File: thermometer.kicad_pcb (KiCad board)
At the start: 2 copper layers, 78.1 x 21.6 mm, 11 parts, among them IC1 ATTINY2313A-P, P1 CONN_4, P2 CONN_4, U1 MC78L05AACP

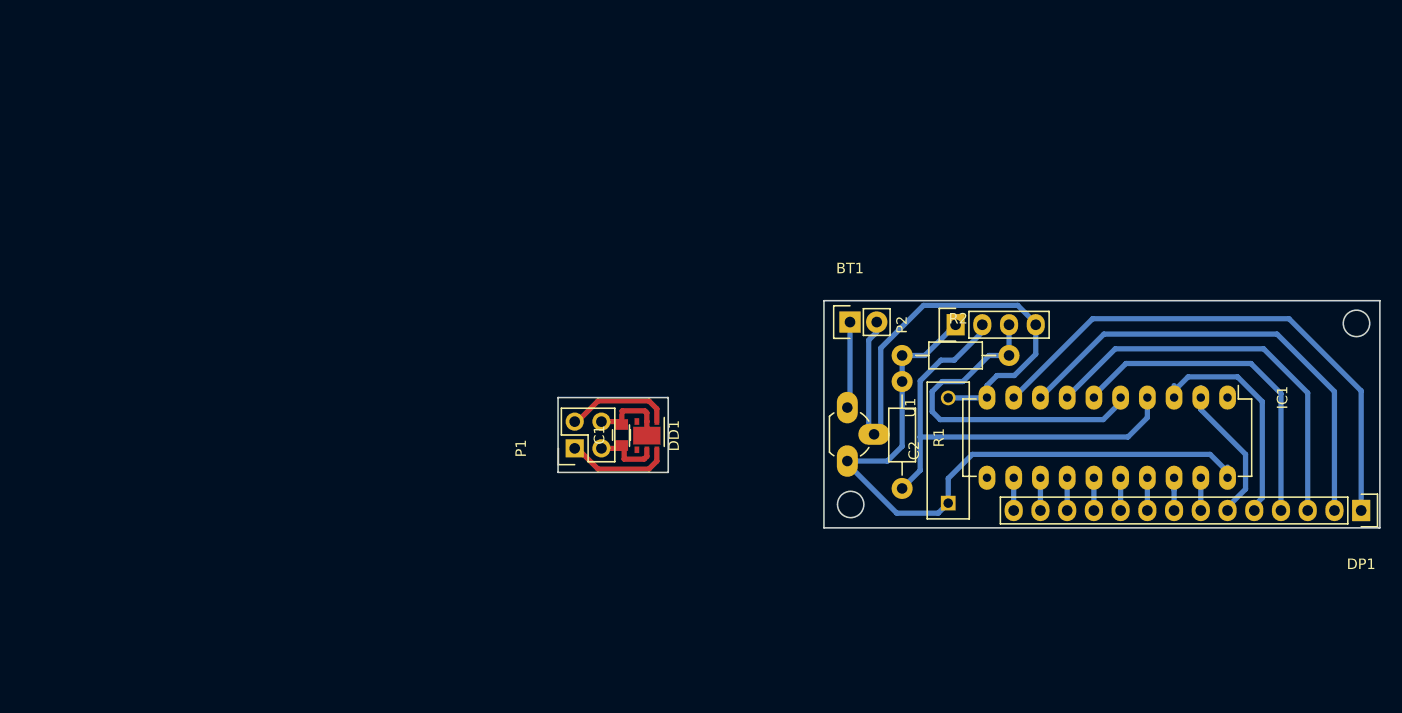
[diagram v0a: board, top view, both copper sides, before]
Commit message: Add I2C functions
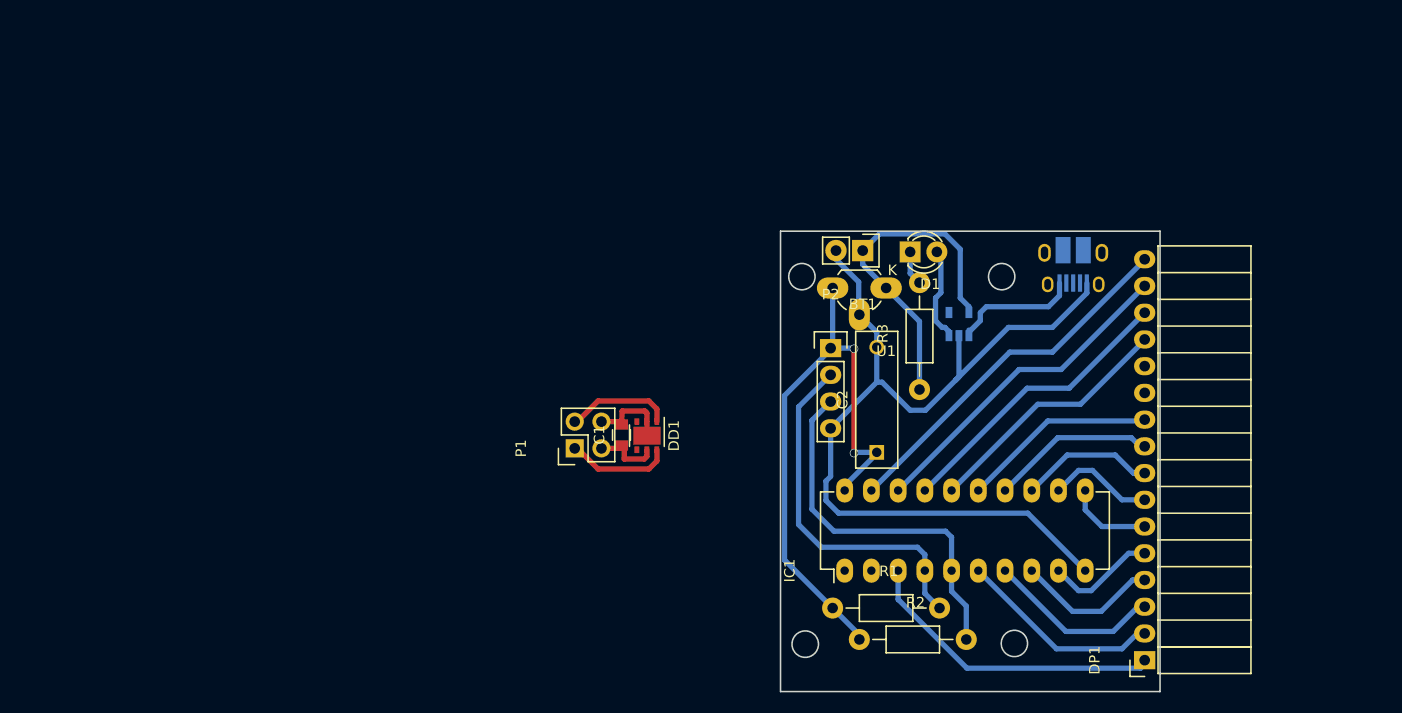
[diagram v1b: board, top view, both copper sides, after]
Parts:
- added D1: LED, LEDs:LED-3MM, F.Cu at (193.1, 96.5)
- added D2: max1555, TO_SOT_Packages_SMD:SOT-23-5, B.Cu at (197.7, 103.4)
- added P3: CONN_5, Connect:USB_Micro-B_10103594-0001LF, B.Cu at (208.6, 98.0)
- added R3: R, Resistors_ThroughHole:Resistor_Horizontal_RM10mm, F.Cu at (194.0, 109.6)
- DP1: footprint Socket_Strips:Socket_Strip_Straight_1x14 -> Socket_Strips:Socket_Strip_Angled_1x16
- moved IC1 39.9 mm to (186.9, 126.8), turned to 90 degrees
- moved R2 27.3 mm to (188.3, 133.3)
- moved DP1 25.0 mm to (215.4, 135.3), turned to 90 degrees
- moved R1 22.5 mm to (185.7, 130.4), turned to 0 degrees
- moved P2 12.1 mm to (185.5, 105.7), turned to 0 degrees
- moved U1 11.9 mm to (190.8, 99.9), turned to 180 degrees
- moved C2 8.33 mm to (189.9, 115.6)
- moved BT1 6.90 mm to (188.6, 96.4), turned to 180 degrees
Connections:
- C1 pad 1: VCC -> VDD
- DD1 pad 5: VCC -> VDD
- DP1 pad 11: Net-(DP1-Pad11) -> (no net)
- DP1 pad 12: Net-(DP1-Pad12) -> (no net)
- IC1 pad 11: (no net) -> Net-(DP1-Pad6)
- IC1 pad 12: Net-(DP1-Pad14) -> Net-(DP1-Pad7)
- IC1 pad 13: Net-(DP1-Pad13) -> Net-(DP1-Pad8)
- IC1 pad 14: Net-(DP1-Pad12) -> Net-(DP1-Pad9)
- IC1 pad 15: Net-(DP1-Pad11) -> Net-(DP1-Pad10)
- IC1 pad 16: Net-(DP1-Pad10) -> Net-(DP1-Pad13)
- IC1 pad 17: Net-(DP1-Pad9) -> Net-(DP1-Pad14)
- IC1 pad 18: Net-(DP1-Pad8) -> Net-(DP1-Pad15)
- IC1 pad 19: Net-(DP1-Pad7) -> Net-(DP1-Pad16)
- IC1 pad 2: Net-(DP1-Pad6) -> (no net)
- IC1 pad 3: Net-(DP1-Pad5) -> Net-(DP1-Pad1)
- IC1 pad 6: Net-(DP1-Pad4) -> Net-(DP1-Pad2)
- IC1 pad 8: Net-(DP1-Pad2) -> Net-(DP1-Pad4)
- IC1 pad 9: Net-(DP1-Pad1) -> Net-(DP1-Pad5)
- P1 pad 3: VCC -> VDD
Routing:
- net Net-(DP1-Pad16): track 0.00 -> 35.2 mm
- net GNDPWR: track 50.8 -> 85.8 mm
- net Net-(DP1-Pad15): track 0.00 -> 31.5 mm
- net Net-(DP1-Pad14): track 3.11 -> 27.9 mm
- net Net-(DP1-Pad2): track 44.0 -> 19.5 mm
- net Net-(BT1-Pad1): track 8.23 -> 32.3 mm
- net Net-(DP1-Pad13): track 3.11 -> 24.4 mm
- net Net-(DP1-Pad3): track 37.7 -> 16.6 mm
- net Net-(DP1-Pad1): track 50.3 -> 29.4 mm
- net Net-(DP1-Pad4): track 31.5 -> 13.6 mm
- net Net-(DP1-Pad10): track 3.11 -> 18.9 mm
- net Net-(DP1-Pad9): track 3.11 -> 15.7 mm
- net Net-(D2-Pad1): track 0.00 -> 12.5 mm
- net Net-(DP1-Pad5): track 22.4 -> 10.5 mm
- net Net-(IC1-Pad4): track 44.5 -> 34.3 mm
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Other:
- board size 78.1 x 21.6 mm -> 36.1 x 43.8 mm

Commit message: Add
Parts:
- added P4: CONN_4, Pin_Headers:Pin_Header_Straight_1x04, F.Cu at (160.7, 82.0)
- added R4: 10k, Resistors_ThroughHole:Resistor_Horizontal_RM7mm, F.Cu at (165.8, 93.6)
- added R5: 10k, Resistors_ThroughHole:Resistor_Horizontal_RM7mm, F.Cu at (168.8, 93.6)
- C2: footprint Capacitors_ThroughHole:C_Rect_L13_W4_P10 -> Capacitors_ThroughHole:C_Rect_L7_W2.5_P5
- DP1: value LCD_Display -> LCD_Display_5; footprint Socket_Strips:Socket_Strip_Angled_1x16 -> Socket_Strips:Socket_Strip_Angled_1x14
- R1, R2, R3: footprint Resistors_ThroughHole:Resistor_Horizontal_RM10mm -> Resistors_ThroughHole:Resistor_Horizontal_RM7mm
- moved C1 52.8 mm to (119.2, 88.8)
- moved DD1 52.8 mm to (121.6, 88.8)
- moved P1 52.8 mm to (114.7, 90.0)
- moved P3 51.4 mm to (158.1, 107.6), turned to 90 degrees
- moved R2 48.9 mm to (159.8, 93.6), turned to 90 degrees
- moved IC1 48.4 mm to (171.8, 80.8), turned to 0 degrees
- moved R1 43.3 mm to (162.8, 93.6), turned to 90 degrees
- moved DP1 39.6 mm to (182.8, 112.9)
- moved P2 36.8 mm to (156.8, 82.8)
- moved D1 35.4 mm to (157.8, 100.0), turned to 90 degrees
- moved D2 34.5 mm to (163.4, 106.3), turned to 0 degrees
- moved R3 29.1 mm to (165.8, 102.6), turned to 180 degrees
- moved BT1 26.1 mm to (166.4, 110.0)
- moved U1 24.0 mm to (167.1, 96.3)
- moved C2 13.7 mm to (179.4, 106.7), turned to 180 degrees
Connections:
- C1 pad 1: VDD -> VCC
- DD1 pad 5: VDD -> VCC
- DP1 pad 11: (no net) -> Net-(DP1-Pad11)
- DP1 pad 12: (no net) -> Net-(DP1-Pad11)
- DP1 pad 6: Net-(DP1-Pad6) -> (no net)
- IC1 pad 11: Net-(DP1-Pad6) -> Net-(DP1-Pad4)
- IC1 pad 12: Net-(DP1-Pad7) -> Net-(DP1-Pad5)
- IC1 pad 13: Net-(DP1-Pad8) -> Net-(DP1-Pad7)
- IC1 pad 14: Net-(DP1-Pad9) -> Net-(DP1-Pad8)
- IC1 pad 15: Net-(DP1-Pad10) -> Net-(DP1-Pad9)
- IC1 pad 16: Net-(DP1-Pad13) -> Net-(DP1-Pad10)
- IC1 pad 17: Net-(DP1-Pad14) -> Net-(DP1-Pad11)
- IC1 pad 18: Net-(DP1-Pad15) -> Net-(DP1-Pad13)
- IC1 pad 19: Net-(DP1-Pad16) -> Net-(DP1-Pad14)
- IC1 pad 2: (no net) -> Net-(IC1-Pad2)
- IC1 pad 3: Net-(DP1-Pad1) -> Net-(IC1-Pad3)
- IC1 pad 6: Net-(DP1-Pad2) -> (no net)
- IC1 pad 7: Net-(DP1-Pad3) -> Net-(DP1-Pad1)
- IC1 pad 8: Net-(DP1-Pad4) -> Net-(DP1-Pad2)
- IC1 pad 9: Net-(DP1-Pad5) -> Net-(DP1-Pad3)
- P1 pad 3: VDD -> VCC
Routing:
- net Net-(DP1-Pad16): track 35.2 -> 0.00 mm
- net Net-(DP1-Pad15): track 31.5 -> 0.00 mm
- net Net-(DP1-Pad14): track 27.9 -> 4.98 mm
- net Net-(DP1-Pad13): track 24.4 -> 4.97 mm
- net VDD: track 63.4 -> 82.8 mm, vias 2 -> 0
- net Net-(IC1-Pad5): track 35.6 -> 19.2 mm
- net GNDPWR: track 85.8 -> 101.7 mm, vias 0 -> 4
- net Net-(DP1-Pad10): track 18.9 -> 3.71 mm
- net Net-(BT1-Pad1): track 32.3 -> 17.3 mm
- net Net-(IC1-Pad4): track 34.3 -> 19.7 mm
- net Net-(IC1-Pad3): track 0.00 -> 12.7 mm
- net Net-(DP1-Pad9): track 15.7 -> 4.66 mm
- net Net-(DP1-Pad4): track 13.6 -> 4.00 mm
- net Net-(IC1-Pad2): track 0.00 -> 9.39 mm
- net Net-(DP1-Pad8): track 12.8 -> 3.71 mm
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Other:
- board size 36.1 x 43.8 mm -> 71 x 36.7 mm

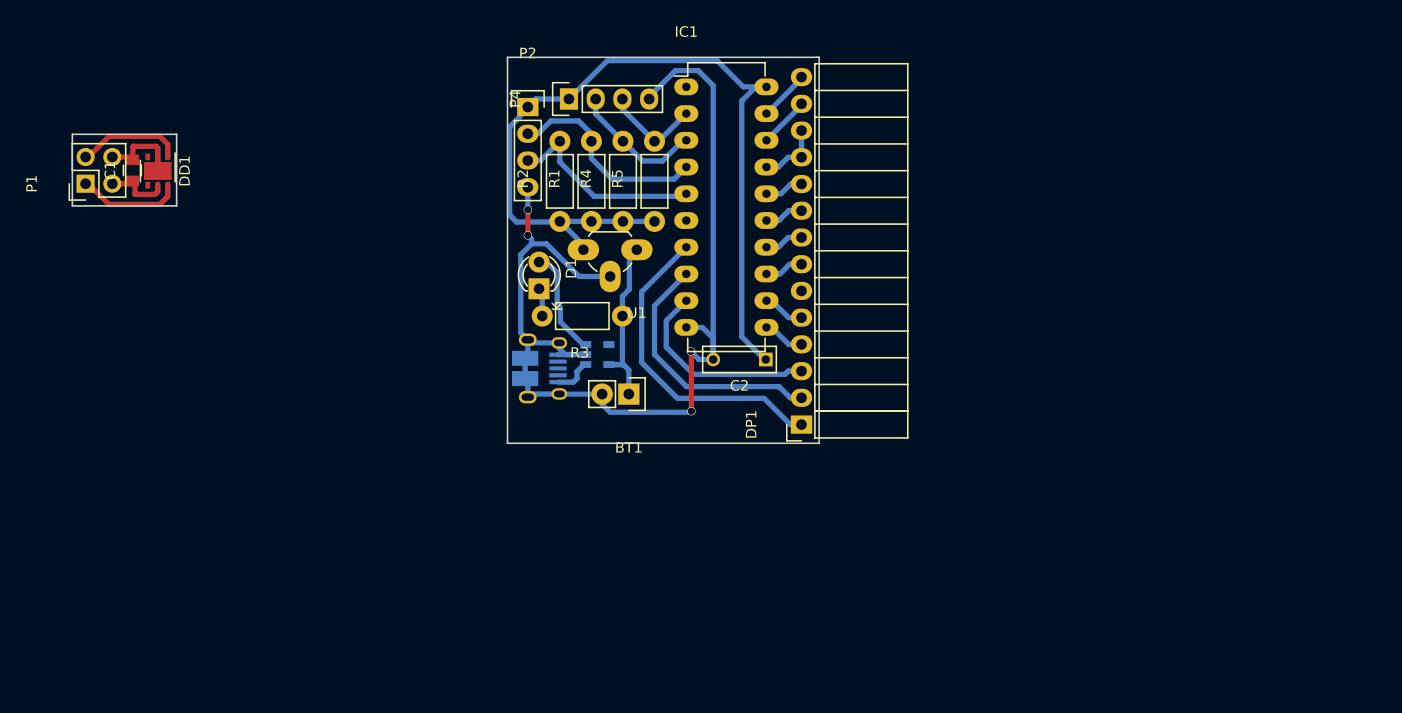
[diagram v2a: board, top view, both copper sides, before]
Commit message: Add ltc1517
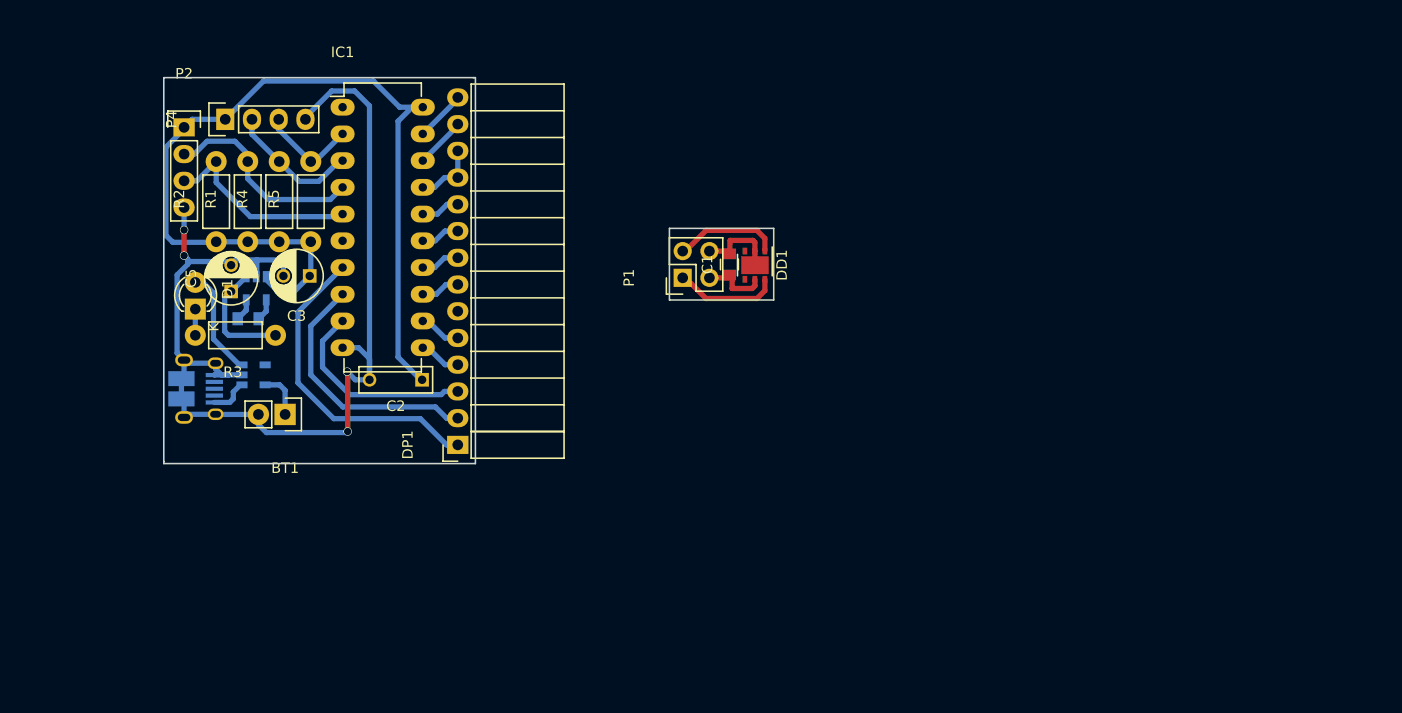
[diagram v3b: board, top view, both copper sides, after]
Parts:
- removed U1: MC78L05AACP, TO_SOT_Packages_THT:TO-92_Rugged
- added C3: 6.8, Capacitors_ThroughHole:C_Radial_D5_L6_P2.5, F.Cu at (136.0, 98.8)
- added C4: 0.1, Capacitors_SMD:C_0805, B.Cu at (130.2, 102.9)
- added C5: 3.3, Capacitors_ThroughHole:C_Radial_D5_L6_P2.5, F.Cu at (128.6, 100.3)
- added DA1: LTC1517, TO_SOT_Packages_SMD:SOT-23-5, B.Cu at (131.0, 100.0)
- C2: value C -> 0.1
- R3: value R -> 330
- moved C1 57.4 mm to (175.9, 97.7)
- moved DD1 57.4 mm to (178.3, 97.8)
- moved P1 57.4 mm to (171.5, 99.0)
- moved R3 33.0 mm to (132.8, 104.4)
- moved BT1 32.7 mm to (133.7, 112.0)
- moved C2 32.7 mm to (146.7, 108.7)
- moved D1 32.7 mm to (125.2, 102.0)
- moved D2 32.7 mm to (130.7, 108.2)
- moved DP1 32.7 mm to (150.1, 114.9)
- moved IC1 32.7 mm to (139.2, 82.8)
- moved P2 32.7 mm to (124.1, 84.7)
- moved P3 32.7 mm to (125.5, 109.5)
- moved P4 32.7 mm to (128.0, 83.9)
- moved R1 32.7 mm to (130.1, 95.6)
- moved R2 32.7 mm to (127.2, 95.6)
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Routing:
- net VDD: track 82.8 -> 87.9 mm
- net GNDPWR: track 101.7 -> 105.2 mm
- net Net-(C4-Pad2): track 0.00 -> 2.13 mm
- net Net-(C4-Pad1): track 0.00 -> 2.09 mm
- net Net-(BT1-Pad1): track 17.3 -> 15.6 mm
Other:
- board size 71 x 36.7 mm -> 58 x 36.7 mm

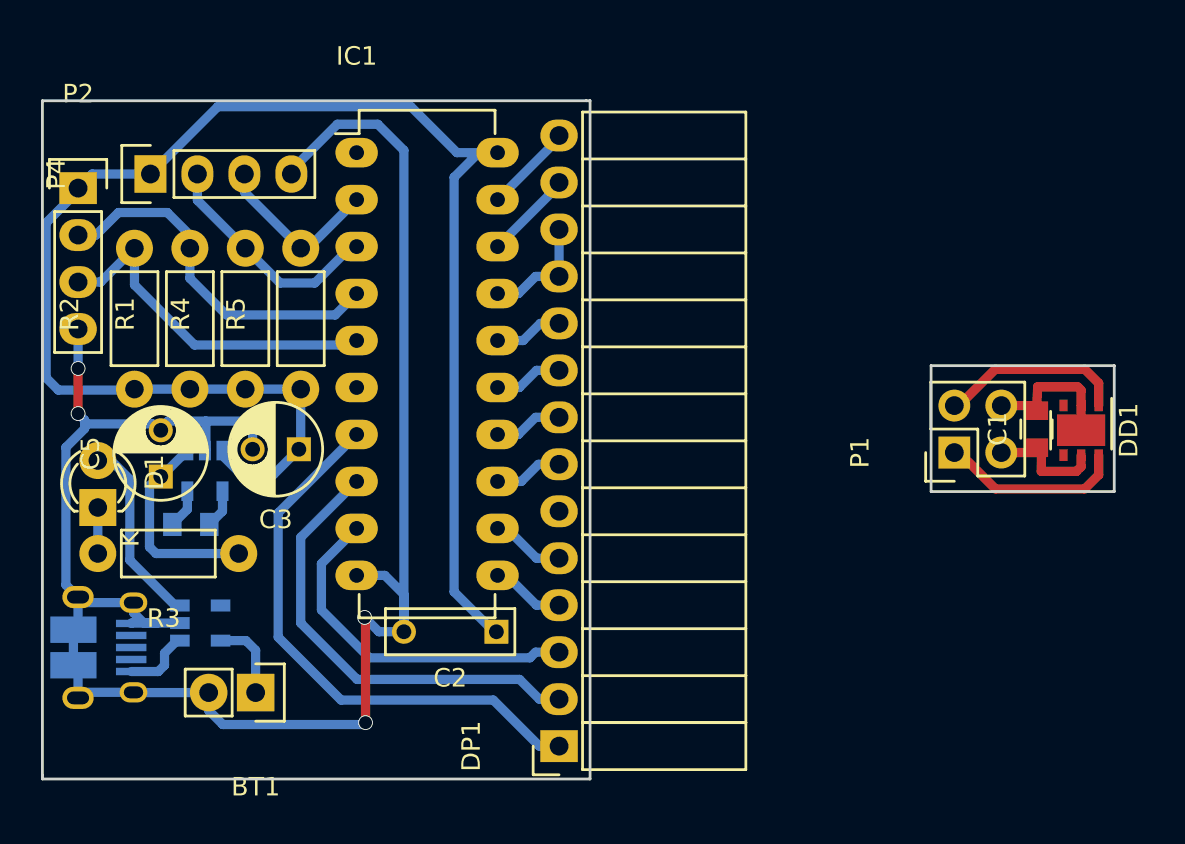
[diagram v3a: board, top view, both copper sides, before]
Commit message: Fix Display
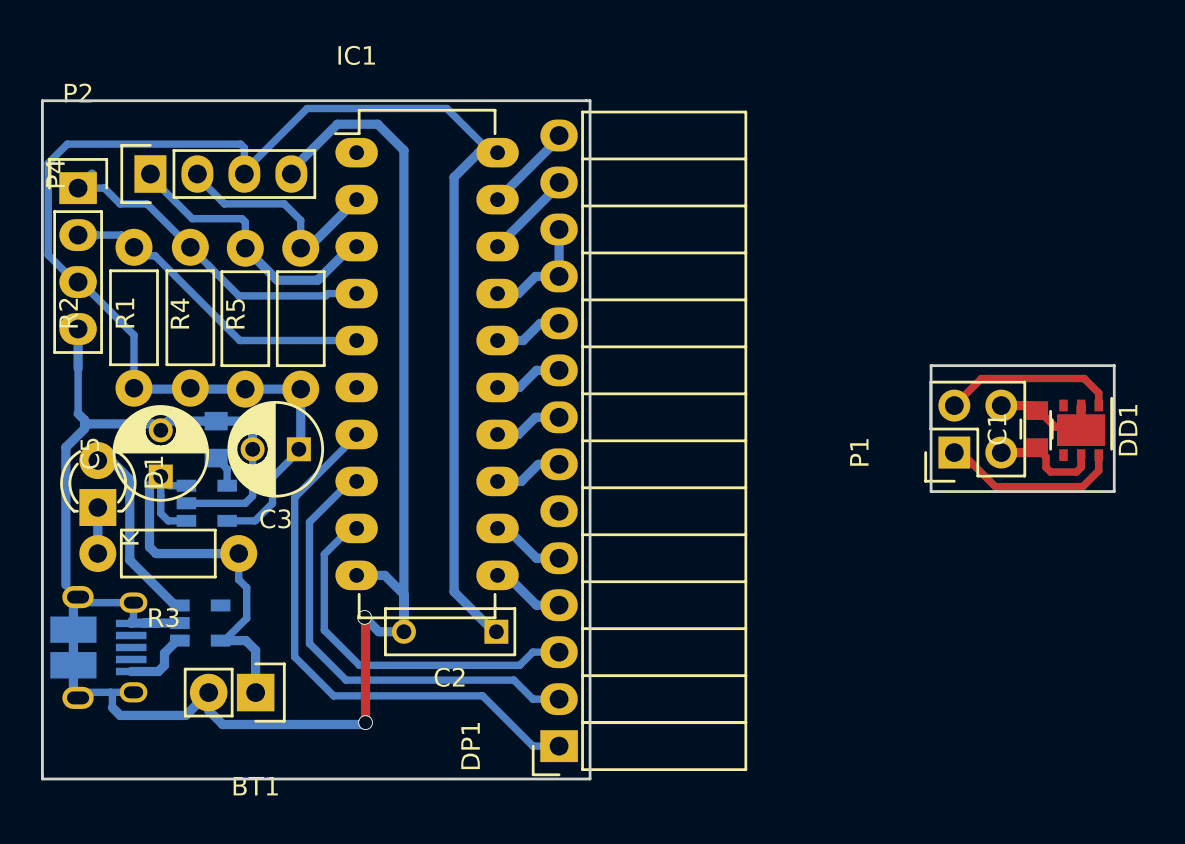
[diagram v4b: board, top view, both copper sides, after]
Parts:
- C3: value 6.8 -> 1.0
- C5: value 3.3 -> 1.0
- DA1: value LTC1517 -> LDK120
- P3: value CONN_5 -> CONN_6
- moved C4 4.79 mm to (131.6, 98.3), turned to 270 degrees
- moved DA1 1.76 mm to (131.1, 101.7), turned to 0 degrees
- moved R1 0.06 mm to (130.2, 95.5)
- moved R2 0.06 mm to (127.1, 95.5)
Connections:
- C4 pad 1: Net-(C4-Pad1) -> GNDPWR
- DA1 pad 3: VDD -> Net-(BT1-Pad1)
- DA1 pad 4: Net-(C4-Pad1) -> Net-(C4-Pad2)
- DA1 pad 5: Net-(C4-Pad2) -> VDD
- P2 pad 1: VDD -> Net-(IC1-Pad4)
- P2 pad 2: Net-(IC1-Pad4) -> Net-(IC1-Pad5)
- P2 pad 3: Net-(IC1-Pad5) -> VDD
- P3 pad 6: (no net) -> GNDPWR
- P4 pad 1: VDD -> Net-(IC1-Pad3)
- P4 pad 2: Net-(IC1-Pad3) -> Net-(IC1-Pad2)
- P4 pad 3: Net-(IC1-Pad2) -> VDD
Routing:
- net Net-(BT1-Pad1): track 15.6 -> 24.2 mm
- net GNDPWR: track 105.2 -> 111.4 mm, vias 4 -> 2
- net Net-(IC1-Pad2): track 9.39 -> 12.3 mm
- net Net-(IC1-Pad3): track 12.7 -> 15.2 mm
- net VDD: track 87.9 -> 90.1 mm
- net Net-(C4-Pad1): track 2.09 -> 0.00 mm
- net Net-(DP1-Pad3): track 20.0 -> 21.0 mm
- net GND: track 8.20 -> 7.36 mm
- net Net-(DD1-Pad1): track 10.1 -> 9.55 mm
- net Net-(IC1-Pad4): track 19.7 -> 19.2 mm
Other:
- net class Default: clearance 0.45 -> 0.4; trace_width 0.5 -> 0.4
- rule trace_clearance: 0.45 -> 0.4
